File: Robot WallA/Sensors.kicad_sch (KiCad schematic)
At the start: 18 parts, among them J34 Conn_01x03, J35 SM04B-SRSS-TB, J36 SM04B-SRSS-TB, J37 SM04B-SRSS-TB, J38 SM02B-SRSS-TB_LF__SN_, J39 Conn_01x03, J40 SM03B-SRSS-TB_LF__SN_, J41 SM03B-SRSS-TB_LF__SN_, J42 SM03B-SRSS-TB_LF__SN_, J43 SM03B-SRSS-TB_LF__SN_, J44 SM02B-SRSS-TB_LF__SN_, J45 SM04B-SRSS-TB, J46 SM02B-SRSS-TB_LF__SN_, J47 SM02B-SRSS-TB_LF__SN_

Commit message: Updated fab files.
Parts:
- J38, J44, J46, J47: footprint SM02BSRSSTBLFSN -> SamacSys_Parts:SM02BSRSSTBLFSN
- J40, J41, J42, J43: footprint SM03BSRSSTBLFSN -> SamacSys_Parts:SM03BSRSSTBLFSN
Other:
- company: (none) -> Socotec Monitoring
- title: (none) -> Robot Wall-A
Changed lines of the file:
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@@
 	(generator_version "9.0")
 	(paper "A4")
+	(title_block
+		(title "Robot Wall-A")
+		(date "2025-09-20")
+		(rev "v1.0")
+		(company "Socotec Monitoring")
+		(comment 1 "GDU")
+		(comment 2 "THO")
+	)
 	(rectangle
 		(start 118.11 96.52)
@@
 			)
 		)
-		(property "Footprint" "SM02BSRSSTBLFSN"
+		(property "Footprint" "SamacSys_Parts:SM02BSRSSTBLFSN"
 			(at 95.25 260.02 0)
 			(effects
@@
 			)
 		)
+		(property "MPN" ""
+			(at 76.2 165.1 0)
+			(effects
+				(font
+					(size 1.27 1.27)
+				)
+				(hide yes)
+			)
+		)
 		(pin "4"
 		)
@@
 			)
 		)
-		(property "Footprint" "SM02BSRSSTBLFSN"
+		(property "Footprint" "SamacSys_Parts:SM02BSRSSTBLFSN"
 			(at 49.53 279.07 0)
 			(effects
@@
 			)
 		)
+		(property "MPN" ""
+			(at 30.48 184.15 0)
+			(effects
+				(font
+					(size 1.27 1.27)
+				)
+				(hide yes)
+			)
+		)
 		(pin "4"
 		)
@@
 			)
 		)
+		(property "MPN" ""
+			(at 142.24 67.31 90)
+			(effects
+				(font
+					(size 1.27 1.27)
+				)
+				(hide yes)
+			)
+		)
 		(pin "2"
 		)
@@
 			)
 		)
+		(property "MPN" ""
+			(at 140.97 120.65 90)
+			(effects
+				(font
+					(size 1.27 1.27)
+				)
+				(hide yes)
+			)
+		)
 		(pin "2"
 		)
@@
 			)
 		)
-		(property "Footprint" "SM03BSRSSTBLFSN"
+		(property "Footprint" "SamacSys_Parts:SM03BSRSSTBLFSN"
 			(at 234.95 23.19 0)
 			(effects
@@
 			)
 		)
+		(property "MPN" ""
+			(at 215.9 118.11 0)
+			(effects
+				(font
+					(size 1.27 1.27)
+				)
+				(hide yes)
+			)
+		)
 		(pin "2"
 		)
@@
 			)
 		)
-		(property "Footprint" "SM02BSRSSTBLFSN"
+		(property "Footprint" "SamacSys_Parts:SM02BSRSSTBLFSN"
 			(at 95.25 279.07 0)
 			(effects
@@
 			)
 		)
+		(property "MPN" ""
+			(at 76.2 184.15 0)
+			(effects
+				(font
+					(size 1.27 1.27)
+				)
+				(hide yes)
+			)
+		)
 		(pin "4"
 		)
@@
 			)
 		)
+		(property "MPN" ""
+			(at 139.7 54.61 0)
+			(effects
+				(font
+					(size 1.27 1.27)
+				)
+				(hide yes)
+			)
+		)
 		(pin "1"
 		)
@@
 			)
 		)
+		(property "MPN" ""
+			(at 130.81 120.65 90)
+			(effects
+				(font
+					(size 1.27 1.27)
+				)
+				(hide yes)
+			)
+		)
 		(pin "2"
 		)
@@
 			)
 		)
+		(property "MPN" ""
+			(at 171.45 78.74 0)
+			(effects
+				(font
+					(size 1.27 1.27)
+				)
+				(hide yes)
+			)
+		)
 		(pin "MP2"
 		)
@@
 			)
 		)
+		(property "MPN" ""
+			(at 140.97 109.22 0)
+			(effects
+				(font
+					(size 1.27 1.27)
+				)
+				(hide yes)
+			)
+		)
 		(pin "1"
 		)
@@
 			)
 		)
+		(property "MPN" ""
+			(at 223.52 58.42 0)
+			(effects
+				(font
+					(size 1.27 1.27)
+				)
+				(hide yes)
+			)
+		)
 		(pin "MP2"
 		)
@@
 			)
 		)
-		(property "Footprint" "SM02BSRSSTBLFSN"
+		(property "Footprint" "SamacSys_Parts:SM02BSRSSTBLFSN"
 			(at 49.53 260.02 0)
 			(effects
@@
 			)
 		)
+		(property "MPN" ""
+			(at 30.48 165.1 0)
+			(effects
+				(font
+					(size 1.27 1.27)
+				)
+				(hide yes)
+			)
+		)
 		(pin "4"
 		)
@@
 			)
 		)
+		(property "MPN" ""
+			(at 132.08 67.31 90)
+			(effects
+				(font
+					(size 1.27 1.27)
+				)
+				(hide yes)
+			)
+		)
 		(pin "2"
 		)
@@
 			)
 		)
+		(property "MPN" ""
+			(at 171.45 58.42 0)
+			(effects
+				(font
+					(size 1.27 1.27)
+				)
+				(hide yes)
+			)
+		)
 		(pin "MP2"
 		)
@@
 			)
 		)
-		(property "Footprint" "SM03BSRSSTBLFSN"
+		(property "Footprint" "SamacSys_Parts:SM03BSRSSTBLFSN"
 			(at 181.61 23.19 0)
 			(effects
@@
 			)
 		)
+		(property "MPN" ""
+			(at 162.56 118.11 0)
+			(effects
+				(font
+					(size 1.27 1.27)
+				)
+				(hide yes)
+			)
+		)
 		(pin "2"
 		)
@@
 			)
 		)
-		(property "Footprint" "SM03BSRSSTBLFSN"
+		(property "Footprint" "SamacSys_Parts:SM03BSRSSTBLFSN"
 			(at 181.61 40.97 0)
 			(effects
@@
 			)
 		)
+		(property "MPN" ""
+			(at 162.56 135.89 0)
+			(effects
+				(font
+					(size 1.27 1.27)
+				)
+				(hide yes)
+			)
+		)
 		(pin "2"
 		)
@@
 			)
 		)
-		(property "Footprint" "SM03BSRSSTBLFSN"
+		(property "Footprint" "SamacSys_Parts:SM03BSRSSTBLFSN"
 			(at 234.95 40.97 0)
 			(effects
@@
 			)
 		)
+		(property "MPN" ""
+			(at 215.9 135.89 0)
+			(effects
+				(font
+					(size 1.27 1.27)
+				)
+				(hide yes)
+			)
+		)
 		(pin "2"
 		)
@@
 				(hide yes)
 			)
+		)
+		(property "MPN" ""
+			(at 223.52 78.74 0)
+			(effects
+				(font
+					(size 1.27 1.27)
+				)
+				(hide yes)
+			)

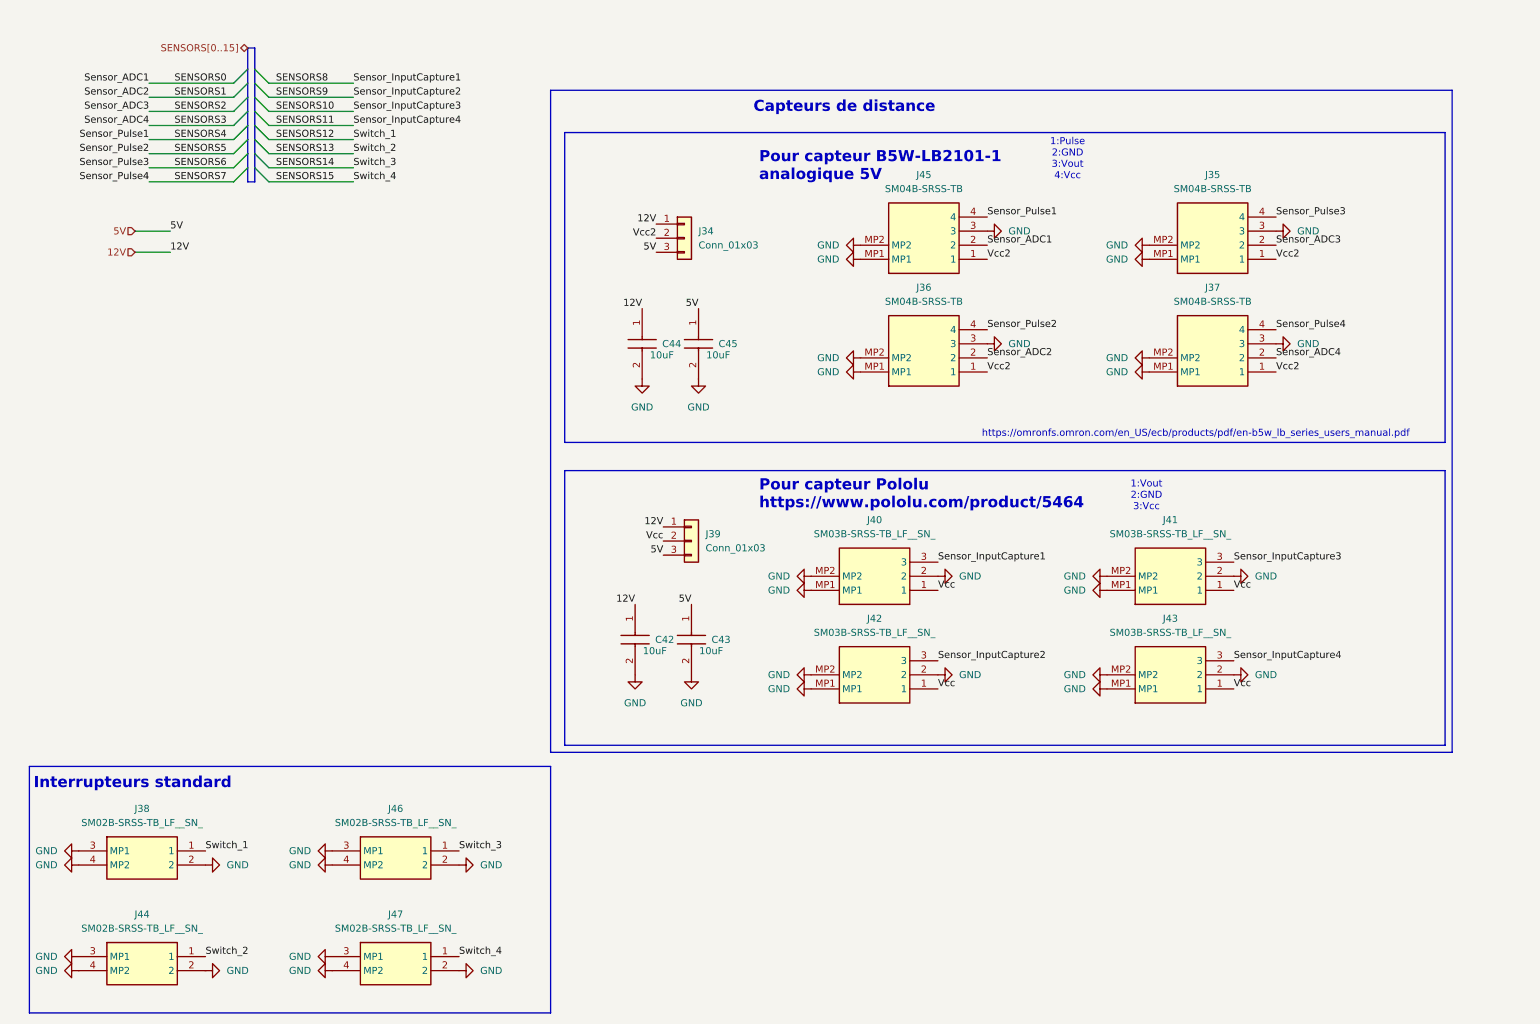
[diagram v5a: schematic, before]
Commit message: Added to BOM connectors and socket
Updated fab files
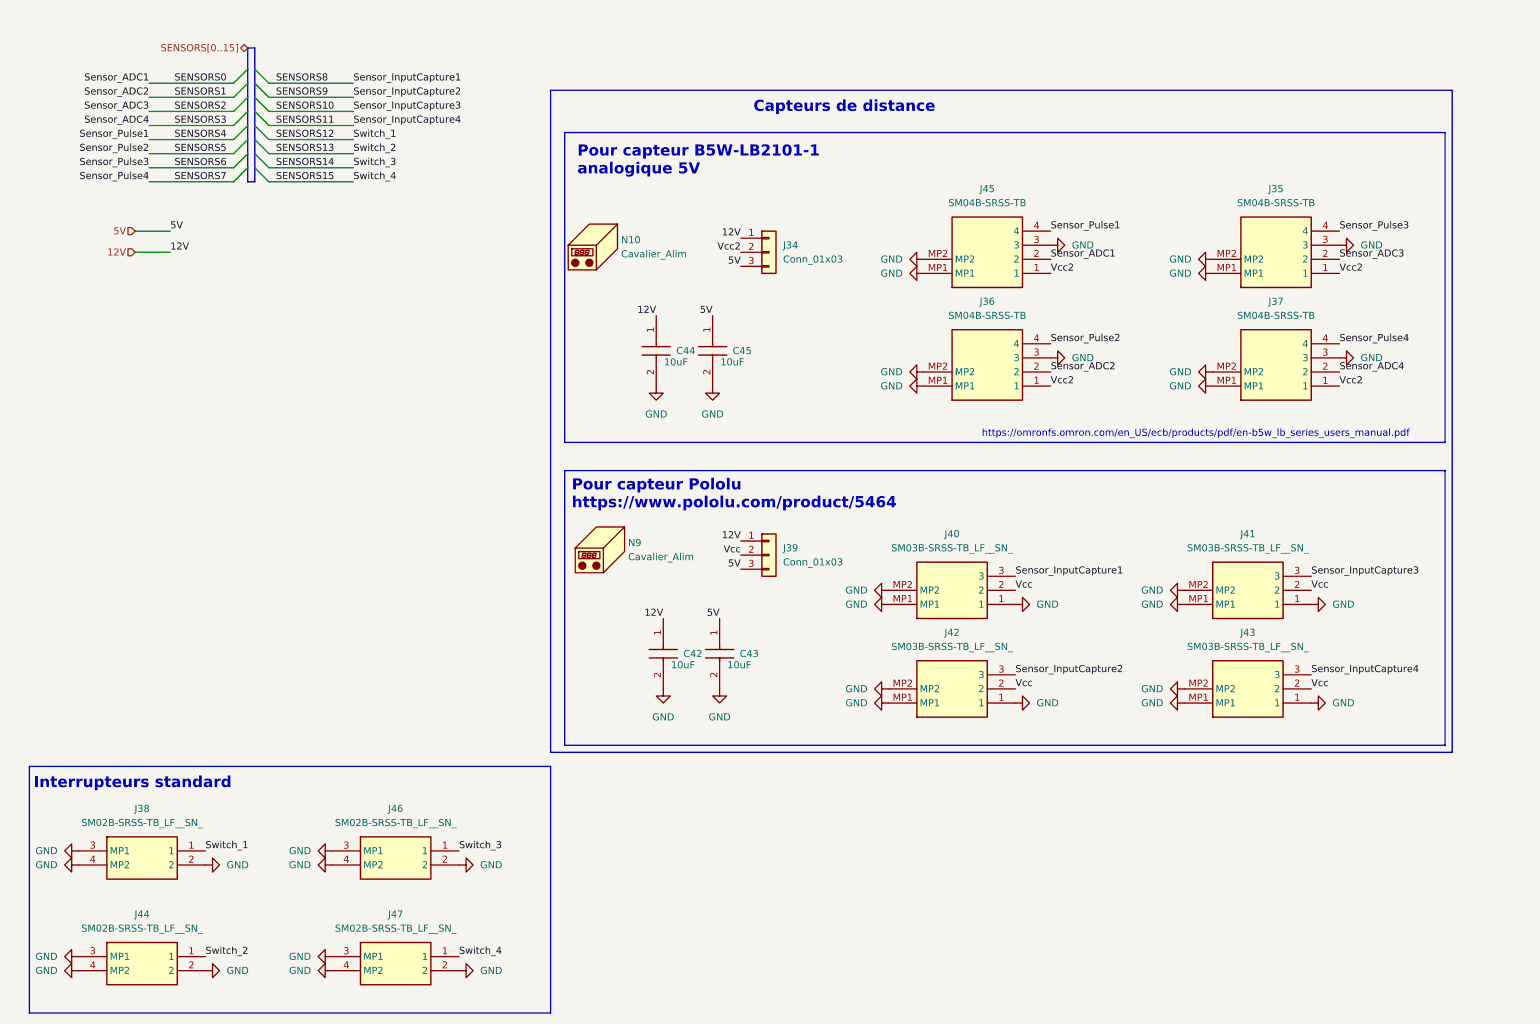
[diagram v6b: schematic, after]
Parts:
- added N10, N9: Cavalier_Alim, symbol Mechanical:Housing
- J38, J44, J46, J47: Arrow Part Number SM02B-SRSS-TB(LF)(SN) -> (none); Arrow Price/Stock https://www.arrow.com/en/products/sm02b-srss-tb-lf-sn/jst-m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 -> (none); Mouser Price/Stock https://www.mouser.co.uk/ProductDetail/JST-Commercial/SM02B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 -> (none)
- J40, J41, J42, J43: Arrow Part Number SM03B-SRSS-TB(LF)(SN) -> (none); Arrow Price/Stock https://www.arrow.com/en/products/sm03b-srss-tb-lf-sn/jst-m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 -> (none); Mouser Price/Stock https://www.mouser.co.uk/ProductDetail/JST-Commercial/SM03B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 -> (none)
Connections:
- net GND: now also J40.1, J41.1, J42.1, J43.1; no longer J40.2, J41.2, J42.2, J43.2
- net Vcc: now also J40.2, J41.2, J42.2, J43.2; no longer J40.1, J41.1, J42.1, J43.1
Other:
- note removed: "1:Pulse 2:GND 3:Vout 4:Vcc"
- note removed: "1:Vout 2:GND 3:Vcc"
- moved on the sheet: C42, C43, C44, C45, J34, J35, J36, J37, J39, J40, J41, J42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

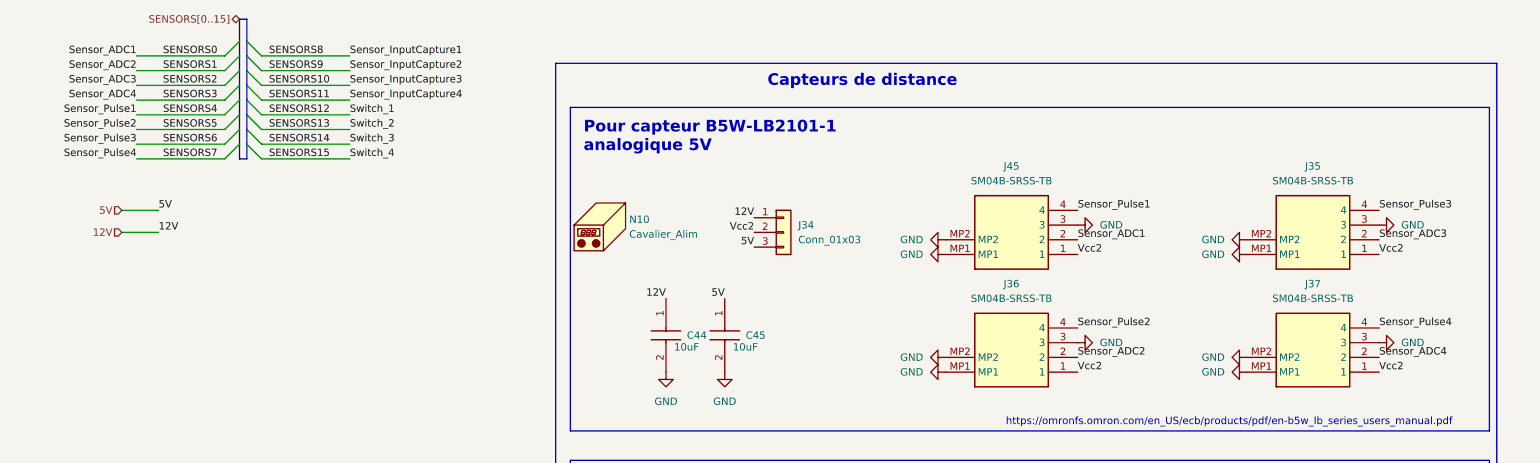
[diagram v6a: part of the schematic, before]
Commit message: Modified a bit pin header pins to allow I2C,SPI and CAN
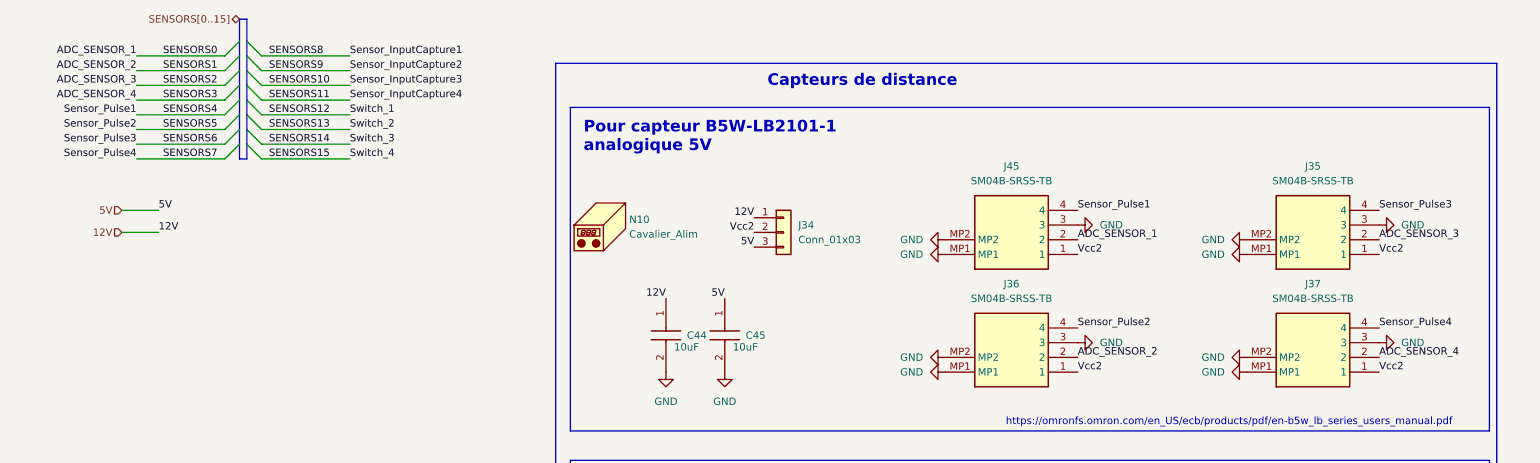
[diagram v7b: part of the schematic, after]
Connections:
- net SENSORS0 renamed ADC_SENSOR_1
- net SENSORS1 renamed ADC_SENSOR_2
- net SENSORS2 renamed ADC_SENSOR_3
- net SENSORS3 renamed ADC_SENSOR_4
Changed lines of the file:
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@@
 		)
 	)
-	(label "Sensor_ADC4"
+	(label "ADC_SENSOR_4"
 		(at 257.81 78.74 0)
 		(effects
@@
 		)
 	)
-	(label "Sensor_ADC2"
+	(label "ADC_SENSOR_2"
 		(at 43.18 29.21 180)
 		(effects
@@
 		)
 	)
-	(label "Sensor_ADC3"
+	(label "ADC_SENSOR_3"
 		(at 257.81 58.42 0)
 		(effects
@@
 		)
 	)
-	(label "Sensor_ADC4"
+	(label "ADC_SENSOR_4"
 		(at 43.18 34.29 180)
 		(effects
@@
 		)
 	)
-	(label "Sensor_ADC2"
+	(label "ADC_SENSOR_2"
 		(at 205.74 78.74 0)
 		(effects
@@
 		)
 	)
-	(label "Sensor_ADC3"
+	(label "ADC_SENSOR_3"
 		(at 43.18 31.75 180)
 		(effects
@@
 		)
 	)
-	(label "Sensor_ADC1"
+	(label "ADC_SENSOR_1"
 		(at 43.18 26.67 180)
 		(effects
@@
 		)
 	)
-	(label "Sensor_ADC1"
+	(label "ADC_SENSOR_1"
 		(at 205.74 58.42 0)
 		(effects

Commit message: Modified footprint to simplify BOM. Finalized BOM.
Updated fab files
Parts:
- C42, C43, C44, C45: Manufacturer_Part_Number (none) -> CL10A106MA8NRNC
- J34, J39: now left out of the parts list
